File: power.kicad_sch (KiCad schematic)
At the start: 12 parts, among them U10 TPS7A7001DDA, U8 TLV75733PDBVR

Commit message: Start ADC work
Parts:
- added TP1, TP2, TP3: TestPoint, symbol Connector:TestPoint
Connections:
- net +3.3V: now also TP2.1
- net +5V: now also TP1.1
- net GND: now also TP3.1

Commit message: Continue work on power supply
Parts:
- added C18: 1000uF, symbol Device:C_Polarized
- added C19: 1uF, symbol Device:C
- added C22: 100nF, symbol Device:C
- added D6: SMBJ5.0A, Diode_SMD:D_SMB, symbol Diode:B220
- added FB1: FerriteBead, symbol Device:FerriteBead
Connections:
- net +5V: now also C19.1, C22.1, D6.1 (K), FB1.2
- net GND: now also C18.2, C19.2, C22.2, D6.2 (A)
- net VBUS: now also C18.1, FB1.1
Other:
- note added: "4.2V regulator - NOTE UPDATE RESISTORS"
- note added: "5V Input filter from BEC"
- note added: "Here's our power scheme: - VBUS is the input from the BEC (battery eliminator circuit) of the ESC. It's full of harmonics and is NOT clean at all. We use this to drive servos and the rest of the power chain. - The 5V net is actually 4.2V. This is because the LDO is used as the final step in filtering the BEC, so there's a voltage drop. The only thing that is being fed by it is the 3.3V regulator,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"
- note added: "MPZ2012S601AT000"
- note removed: "5V regulator"
- moved on the sheet: C20, C21, R22, R23, U10

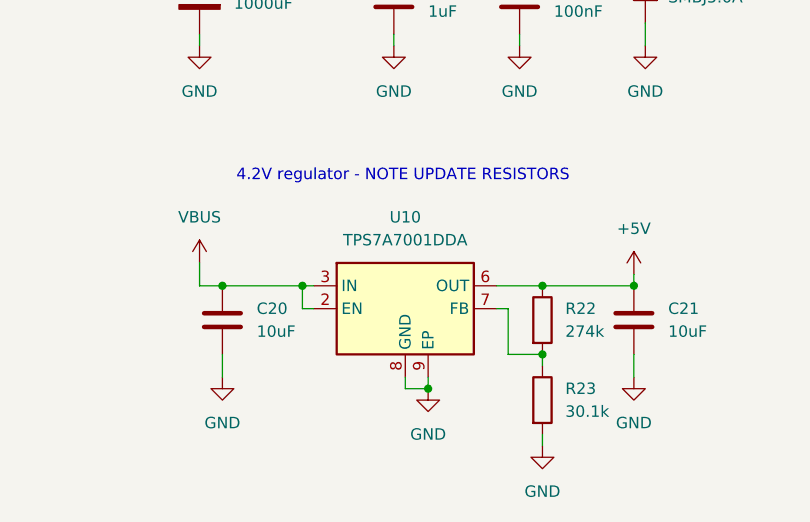
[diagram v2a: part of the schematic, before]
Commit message: 4.2V Regulator design
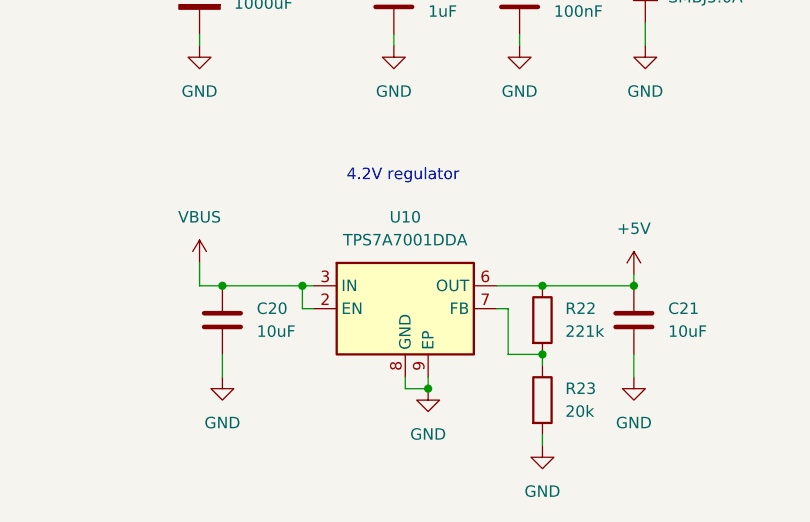
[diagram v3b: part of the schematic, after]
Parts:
- R22: value 274k -> 221k
- R23: value 30.1k -> 20k
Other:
- note added: "4.2V regulator"
- note removed: "4.2V regulator - NOTE UPDATE RESISTORS"
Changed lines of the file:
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@@
 	(generator_version "9.0")
 	(paper "A4")
-	(text "4.2V regulator - NOTE UPDATE RESISTORS"
+	(text "4.2V regulator"
 		(exclude_from_sim no)
 		(at 100.076 135.128 0)
@@
 			)
 		)
-		(property "Value" "274k"
+		(property "Value" "221k"
 			(at 118.11 152.3999 0)
 			(effects
@@
 			)
 		)
-		(property "Value" "30.1k"
+		(property "Value" "20k"
 			(at 118.11 161.2899 0)
 			(effects

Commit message: Work more on power
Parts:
- added D5: LED, symbol Device:LED
- added R40: 470R, symbol Device:R
- added TP4: TestPoint, symbol Connector:TestPoint
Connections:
- net +5V: now also C16.1, U8.1 (IN), U8.3 (EN); no longer C19.1, C22.1, D6.1 (K), FB1.2
- net GND: now also R40.2
- net VBUS: now also D5.2 (A), TP4.1; no longer C16.1, C20.1, U10.2 (EN), U10.3 (IN), U8.1 (IN), U8.3 (EN)
- new net: D5.1 (K), R40.1
- new net VBUS_Filtered: C19.1, C20.1, C22.1, D6.1 (K), FB1.2, U10.2 (EN), U10.3 (IN)
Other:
- note added: "->"
- moved on the sheet: C16, C17, C18, C19, C20, C21, C22, D2, D3, D6, FB1, R20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

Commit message: Work on power supply...
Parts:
- removed C20: 10uF, symbol Device:C
- removed D6: SMBJ5.0A, Diode_SMD:D_SMB, symbol Diode:B220
- added C23: 3300uF, symbol Device:C_Polarized
- added L2: 15uH, symbol Device:L
- C18: value 1000uF -> 470uF
- C19: value 1uF -> 10uF
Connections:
- net GND: now also C23.2
- net VBUS: now also L2.1; no longer FB1.1
- new net: C23.1, FB1.1, L2.2
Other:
- note added: "APH0630T150M"
- note added: "Cap omitted here because of previous caps"
- note added: "Filter curve"
- note added: "Input bulk (pre-LC) Cin: 100-470 µF electrolytic Purpose: absorb ESC current spikes Voltage: ≥ 2× battery max ESR: not critical Main LC low-pass L1: 33 µH shielded power inductor DCR ≈ 0.27 Ω (good - provides damping) Current rating: ≥ 2× max rail current Saturation current: ≥ 2.5× load C1: 3300 µF electrolytic Voltage: ≥ 2× rail voltage ESR: 20-100 mΩ (perfect) 🧠 Results: Cutoff frequency ≈ 480 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"
- note added: "LC Filter ~700Hz"
- note added: "Low frequency filter cap"
- moved on the sheet: C18, C19, C22, FB1

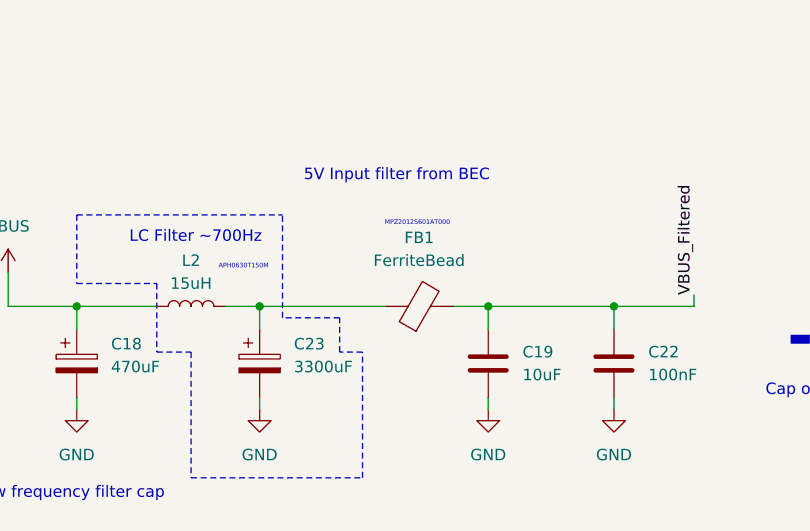
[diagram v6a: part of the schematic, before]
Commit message: More work... SD, flash, etc.
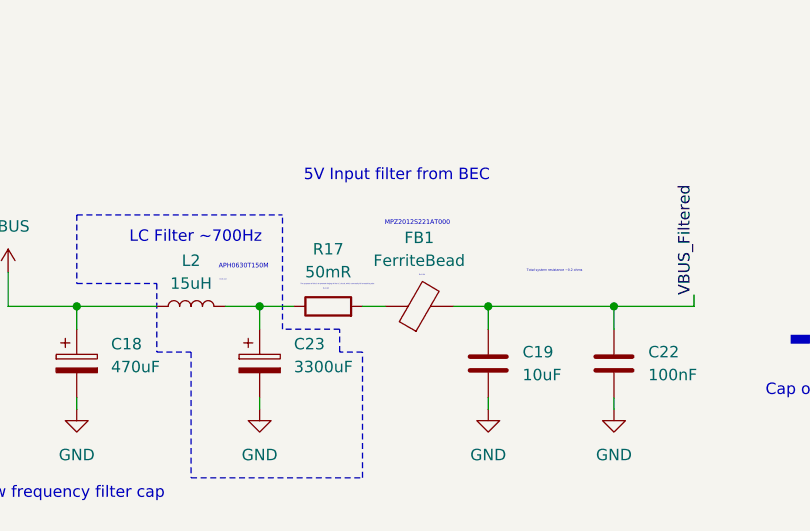
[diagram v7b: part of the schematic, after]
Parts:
- added R17: 50mR, symbol Device:R
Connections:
- net at C23.1, L2.2: now also R17.1; no longer FB1.1
- new net: FB1.1, R17.2
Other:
- note added: "MPZ2012S221AT000"
- note added: "R=0.04"
- note added: "R=0.05"
- note added: "R=0.113"
- note added: "The purpose of this is to prevent ringing of the LC circuit, which can easily kill everything else"
- note added: "Total system resistance ~0.2 ohms"
- note removed: "MPZ2012S601AT000"
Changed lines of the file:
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@@
 		)
 	)
+	(text "R=0.04"
+		(exclude_from_sim no)
+		(at 70.104 133.858 0)
+		(effects
+			(font
+				(size 0.127 0.127)
+			)
+		)
+	)
+	(text "R=0.113"
+		(exclude_from_sim no)
+		(at 48.006 134.366 0)
+		(effects
+			(font
+				(size 0.127 0.127)
+			)
+		)
+	)
 	(text "Supply Indicator"
 		(exclude_from_sim no)
@@
 		)
 	)
+	(text "R=0.05"
+		(exclude_from_sim no)
+		(at 59.436 135.382 0)
+		(effects
+			(font
+				(size 0.127 0.127)
+			)
+		)
+	)
 	(text "Filter curve"
 		(exclude_from_sim no)
@@
 		)
 	)
+	(text "Total system resistance ~0.2 ohms"
+		(exclude_from_sim no)
+		(at 84.836 133.35 0)
+		(effects
+			(font
+				(size 0.254 0.254)
+			)
+		)
+	)
 	(text "APH0630T150M"
 		(exclude_from_sim no)
@@
 		)
 	)
-	(text "MPZ2012S601AT000"
+	(text "MPZ2012S221AT000\n"
 		(exclude_from_sim no)
 		(at 69.596 128.016 0)
@@
 		)
 	)
+	(text "The purpose of this is to prevent ringing of the LC circuit, which can easily kill everything else"
+		(exclude_from_sim no)
+		(at 60.706 134.874 0)
+		(effects
+			(font
+				(size 0.127 0.127)
+			)
+		)
+	)
 	(text "->"
 		(exclude_from_sim no)
@@
 	)
 	(junction
-		(at 177.8 135.89)
+		(at 52.07 137.16)
 		(diameter 0)
 		(color 0 0 0 0)
 	)
 	(junction
-		(at 140.97 135.89)
+		(at 177.8 135.89)
 		(diameter 0)
 		(color 0 0 0 0)
 	)
 	(junction
-		(at 167.64 135.89)
+		(at 140.97 135.89)
 		(diameter 0)
 		(color 0 0 0 0)
 	)
 	(junction
-		(at 52.07 137.16)
+		(at 167.64 135.89)
 		(diameter 0)
 		(color 0 0 0 0)
@@
 	(polyline
 		(pts
-			(xy 60.96 142.24) (xy 60.96 138.43)
+			(xy 60.96 142.24) (xy 60.96 139.7)
 		)
 		(stroke
@@
 	(wire
 		(pts
-			(xy 232.41 138.43) (xy 232.41 135.89)
+			(xy 63.5 137.16) (xy 66.04 137.16)
 		)
 		(stroke
@@
 		)
 	)
-	(polyline
+	(wire
 		(pts
-			(xy 31.75 127) (xy 31.75 134.62)
+			(xy 232.41 138.43) (xy 232.41 135.89)
 		)
 		(stroke
 			(width 0)
-			(type dash_dot)
+			(type default)
 		)
 	)
 	(polyline
 		(pts
-			(xy 40.64 142.24) (xy 44.45 142.24)
+			(xy 31.75 127) (xy 31.75 134.62)
 		)
 		(stroke
@@
 		)
 	)
-	(wire
+	(polyline
 		(pts
-			(xy 222.25 143.51) (xy 222.25 146.05)
+			(xy 40.64 142.24) (xy 44.45 142.24)
 		)
 		(stroke
 			(width 0)
-			(type default)
+			(type dash_dot)
 		)
 	)
 	(wire
 		(pts
-			(xy 66.04 137.16) (xy 52.07 137.16)
+			(xy 222.25 143.51) (xy 222.25 146.05)
 		)
 		(stroke
@@
 	(polyline
 		(pts
-			(xy 60.96 138.43) (xy 54.61 138.43)
+			(xy 60.96 139.7) (xy 54.61 139.7)
 		)
 		(stroke
@@
 	(wire
 		(pts
+			(xy 55.88 137.16) (xy 52.07 137.16)
+		)
+		(stroke
+			(width 0)
+			(type default)
+		)
+	)
+	(wire
+		(pts
 			(xy 167.64 135.89) (xy 177.8 135.89)
 		)
@@
 	(polyline
 		(pts
-			(xy 54.61 138.43) (xy 54.61 127)
+			(xy 54.61 139.7) (xy 54.61 127)
 		)
 		(stroke
@@
 					(unit 1)
 				)
+			)
+		)
+	)
+	(symbol
+		(lib_id "Device:R")
+		(at 59.69 137.16 90)
+		(unit 1)
+		(exclude_from_sim no)
+		(in_bom yes)
+		(on_board yes)
+		(dnp no)
+		(fields_autoplaced yes)
+		(property "Reference" "R17"
+			(at 59.69 130.81 90)
+			(effects
+				(font
+					(size 1.27 1.27)
+				)
+			)
+		)
+		(property "Value" "50mR"
+			(at 59.69 133.35 90)
+			(effects
+				(font
+					(size 1.27 1.27)
+				)
+			)
+		)
+		(property "Footprint" ""
+			(at 59.69 138.938 90)
+			(effects
+				(font
+					(size 1.27 1.27)
+				)
+				(hide yes)
+			)
+		)
+		(property "Datasheet" "~"
+			(at 59.69 137.16 0)
+			(effects
+				(font
+					(size 1.27 1.27)
+				)
+				(hide yes)
+			)
+		)
+		(property "Description" "Resistor"
+			(at 59.69 137.16 0)
+			(effects
+				(font
+					(size 1.27 1.27)
+				)
+				(hide yes)
+			)
+		)
+		(pin "1"
+		)
+		(pin "2"
+		)
+		(instances
+			(project ""
+				(path "/e99ca14d-cacc-4390-92ee-6dcff8e13ef3/b4a2b830-aa8f-41e8-96c4-9a049628082b"
+					(reference "R17")
+					(unit 1)
+				)

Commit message: Initial routing
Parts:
- TP1, TP2, TP3, TP4: footprint (none) -> TestPoint:TestPoint_Pad_D2.0mm
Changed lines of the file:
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@@
 			)
 		)
-		(property "Footprint" ""
+		(property "Footprint" "TestPoint:TestPoint_Pad_D2.0mm"
 			(at 92.71 55.88 0)
 			(effects
@@
 			)
 		)
-		(property "Footprint" ""
+		(property "Footprint" "TestPoint:TestPoint_Pad_D2.0mm"
 			(at 124.46 55.88 0)
 			(effects
@@
 			)
 		)
-		(property "Footprint" ""
+		(property "Footprint" "TestPoint:TestPoint_Pad_D2.0mm"
 			(at 109.22 55.88 0)
 			(effects
@@
 			)
 		)
-		(property "Footprint" ""
+		(property "Footprint" "TestPoint:TestPoint_Pad_D2.0mm"
 			(at 138.43 55.88 0)
 			(effects
